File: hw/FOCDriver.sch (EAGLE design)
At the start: 111 parts, among them Q1 BC817, Q2 BC817, Q3 BC817, Q4 BC817, Q5 BC817, Q6 BC817, U1 IRF9389TRPBF, U2 IRF9389TRPBF, U3 LM27313XMF, U4 IRF9389TRPBF, U5 LM358N, U6 LM358N, U7 SN74LVC1G17, U8 SN74LVC1G17, U9 SN74LVC1G17

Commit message: layout
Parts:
- removed U7, U8, U9: SN74LVC1G17, SN74LVC1G17:SN74LVC1G17
- added U10, U11, U12: SN74LVC2G17, SN74LVC:SN74LVC2G17
- R17, R2, R9: value 100 -> 1K
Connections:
- new net N$49: R1.1, R3.1, U10G$2.Y
- new net N$50: R10.1, R8.1, U11G$2.Y
- new net N$51: R16.1, R18.1, U12G$2.Y
- net +5V: now also U10G$1.VCC, U11G$1.VCC, U12G$1.VCC; no longer U7.VCC, U8.VCC, U9.VCC
- net GND: now also U10G$1.GND, U11G$1.GND, U12G$1.GND; no longer U7.GND, U8.GND, U9.GND
- net H1: now also U10G$2.A; no longer R1.1, R3.1
- net H2: now also U11G$2.A; no longer R10.1, R8.1
- net H3: now also U12G$2.A; no longer R16.1, R18.1
- net L1: now also U10G$1.A; no longer U7.A
- net L2: now also U11G$1.A; no longer U8.A
- net L3: now also U12G$1.A; no longer U9.A
- net N$46: now also U10G$1.Y; no longer U7.Y
- net N$47: now also U11G$1.Y; no longer U8.Y
- net N$48: now also U12G$1.Y; no longer U9.Y
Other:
- moved on the sheet: C1, Q1, Q2, R1, R10, R17, R18, R2, R3, R4, R5, R6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

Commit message: layout
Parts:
- removed C9: 1nF, SparkFun-Capacitors:1.0UF-0805-25V-10%
- removed J1: (no value), SparkFun-Connectors:CONN_08"
- removed U2, U4: IRF9389TRPBF, IRF9389TRPBF:IRF9389TRPBF
- added C13: 47uF, rcl:CPOL-USE2.5-7
- added C14, C31: 0.1uF, SparkFun-Capacitors:1.0UF-0805-25V-10%
- added C2, C3, C6: 10uF, SparkFun-Capacitors:1.0UF-0805-25V-10%
- added C7: 100uF, rcl:CPOL-USE2.5-7
- added J3: (no value), SparkFun-Connectors:CONN_06SILK_FEMALE_PTH
- added U7, U8, U9: AO4606, AO4606:AO4606
- C10: value 4.7uF -> 0.1uF
- C11: value 470uF -> 47uF
- C19, C20: value 0.1uF -> 10uF
- R53: value 3.3K -> 1K
- U1: value IRF9389TRPBF -> SPX1117-5.0; device IRF9389TRPBF:IRF9389TRPBF -> SparkFun-IC-Power:V_REG_317SMD
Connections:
- removed net N$46: R2.1, U10G$1.Y
- removed net N$47: R9.1, U11G$1.Y
- removed net N$48: R17.1, U12G$1.Y
- removed net N$49: R1.1, R3.1, U10G$2.Y
- removed net N$50: R10.1, R8.1, U11G$2.Y
- removed net N$51: R16.1, R18.1, U12G$2.Y
- new net +3V3: J2.2, R54.E
- new net H1O: R1.1, R3.1, R45.2, U10G$2.Y
- new net H2O: R10.1, R49.2, R8.1, U11G$2.Y
- new net H3O: R16.1, R18.1, R51.2, U12G$2.Y
- new net L1O: R2.1, R46.2, U10G$1.Y
- new net L2O: R50.2, R9.1, U11G$1.Y
- new net L3O: R17.1, R52.2, U12G$1.Y
- net +12V: now also C31.1, U1.IN, U7A.S, U8A.S, U9A.S; no longer C9.1, U1A.S, U2A.S, U4A.S
- net +5V: now also C13.+, C14.1, C2.1, C3.1, C6.1, U1.OUT; no longer J2.1, R54.E
- net AGND: now also C13.-, C14.2, C31.2, C7.-, U1.ADJ; no longer C9.2
- net GND: now also C2.2, C3.2, C6.2, J2.1, J3.6; no longer J1.7, J1.8, J2.2
- net H1: no longer R45.2
- net H2: no longer R49.2
- net H3: no longer R51.2
- net ICOM: now also U9B.S; no longer U4B.S
- net IMOTORA: now also J3.3; no longer J1.3
- net IMOTORB: now also J3.2; no longer J1.2
- net IMOTORBUS: now also J3.1; no longer J1.1
- net IU: now also U7B.S; no longer U1B.S
- net IV: now also U8B.S; no longer U2B.S
- net L1: no longer R46.2
- net L2: no longer R50.2
- net L3: no longer R52.2
- net LEDJP1: now also J3.5; no longer J1.6
- net M1: now also U7A.D, U7B.D; no longer U1A.D, U1B.D
- net M2: now also U8A.D, U8B.D; no longer U2A.D, U2B.D
- net M3: now also U9A.D, U9B.D; no longer U4A.D, U4B.D
- net N$1: now also C7.+
- net N$10: now also U7A.G; no longer U1A.G
- net N$3: now also U9B.G; no longer U4B.G
- net N$6: now also U9A.G; no longer U4A.G
- net N$7: now also U8B.G; no longer U2B.G
- net N$8: now also U8A.G; no longer U2A.G
- net N$9: now also U7B.G; no longer U1B.G
- net POT: now also J3.4; no longer J1.5
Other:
- moved on the sheet: C1, C12, C5, C8, D1, F1, LED7, Q1, Q2, Q3, Q4, Q5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

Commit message: layout
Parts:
- removed C1, C12, C5: 10uF, SparkFun-Capacitors:1.0UF-0805-25V-10%
- removed C30: 0.1uF, SparkFun-Capacitors:1.0UF-0805-25V-10%
- removed C7: 100uF, rcl:CPOL-USE2.5-7
- removed C8: 220pF, SparkFun-Capacitors:1.0UF-0805-25V-10%
- removed L1: 10uH, resistor:L-USL3225M
- removed LED8: 12V, led:LEDSML0805
- removed R15: 118K, SparkFun-Resistors:RESISTOR0805
- removed R56: 10K, SparkFun-Resistors:RESISTOR0805
- removed U1: SPX1117-5.0, SparkFun-IC-Power:V_REG_317SMD
- removed U3: LM27313XMF, LM27313XMF:LM27313XMF
- added C32, C33: 220uF/100V, rcl:CPOL-USE5-10.5
- added J1: (no value), SparkFun-Connectors:CONN_02
- added Q7: IRFR5305, transistor-power:IRFR5305
- added U2: BA7805FP, SparkFun-IC-Power:V_REG_78XX7812
- C19, C2, C20, C3, C6: value 10uF -> 0.1uF
- C21, C22, C23: value 0.1uF -> 100pF
- C4: value 10uF -> 220uF/100V; device SparkFun-Capacitors:1.0UF-0805-25V-10% -> rcl:CPOL-USE5-10.5
- D1: value MBR0520LT -> MM3Z18VT1G; device diode:MBR0520LT -> SparkFun-DiscreteSemi:DIODE-ZENER-MM3Z3V3T1G
- F1: value 16V/4.00A -> 4A/30V
- R14: value 13.3K -> 22.6K
- R34, R35, R36, R37, R38, R39, R40, R41: value 30K 1% -> 20K 1%
- R53: value 1K -> 3.3K
- R54: value (none) -> 10K
- R55: value 1K -> 5.6K
- R7: value 51K -> 100K
- renumbered LED7 to 5VPWR
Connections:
- removed net +12V: C1.1, C10.1, C11.+, C12.1, C31.1, C5.1, C8.2, D1.C, R11.2, R15.2, R19.2, R4.2, R56.2, U1.IN, U7A.S, U8A.S, U9A.S
- removed net +3V3: J2.2, R54.E
- removed net N$29: C30.1, R54.A, R55.2
- removed net N$45: LED8.A, R56.1
- removed net N$5 (its old number): D1.A, L1.1, U3.SW
- new net VCC: C10.1, C11.+, C31.1, C32.+, C33.+, C4.+, D1.C, J1.2, Q7.S, R11.2, R19.2, R4.2, R7.2, U2.IN, U7A.S, U8A.S, U9A.S
- net +5V: now also R55.2, U2.OUT; no longer U1.OUT
- net AGND: now also C32.-, C33.-, C4.-, U2.GND; no longer C21.2, C22.2, C23.2, C4.2, C7.-, LED8.C, U1.ADJ, U3.GND
- net GND: now also J2.2, R54.A; no longer C30.2, R55.1
- net N$1: now also J1.1, Q7.D; no longer C4.1, C7.+, L1.2, R7.1, U3.VIN
- net N$10: no longer C1.2
- net N$15: now also C21.2
- net N$2: now also D1.A, Q7.G, R14.2, R7.1; no longer R7.2, U3.!SHDN!
- net N$20: now also C22.2
- net N$25: now also C23.2
- net N$4: now also R54.E, R55.1; no longer C8.1, R14.2, R15.1, U3.FB
- net N$6: no longer C12.2
- net N$8: no longer C5.2
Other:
- note added: "0~3.2V"
- note added: "Gain: I * 0.025 * 20k / 1k = 0.5 V/A FS Current = 2.5V / 0.5V/A = +/-5A F = 1/ 2 * Pi * 20k * 100pF"
- note added: "VREF: 5V * 20k / 40k = 2.5V F = 1/ 2 * Pi * 20k||20k * 100nF"
- moved on the sheet: C10, C11, C13, C14, C18, C21, C22, C23, C31, D1, F1, R14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

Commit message: layout
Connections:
- new net VDD: C19.1, U5G$3.VCC
- net AVDD: no longer C19.1, U5G$3.VCC
- net N$19: now also U6G$1.-IN; no longer U5G$1.-IN
- net N$20: now also U6G$1.+IN; no longer U5G$1.+IN
- net N$21: now also U6G$1.OUT; no longer U5G$1.OUT
- net N$24: now also U5G$1.-IN; no longer U6G$1.-IN
- net N$25: now also U5G$1.+IN; no longer U6G$1.+IN
- net N$26: now also U5G$1.OUT; no longer U6G$1.OUT
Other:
- moved on the sheet: C16, C17, C20, C21, C22, C25, C26, R24, R25, R26, R27, R30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

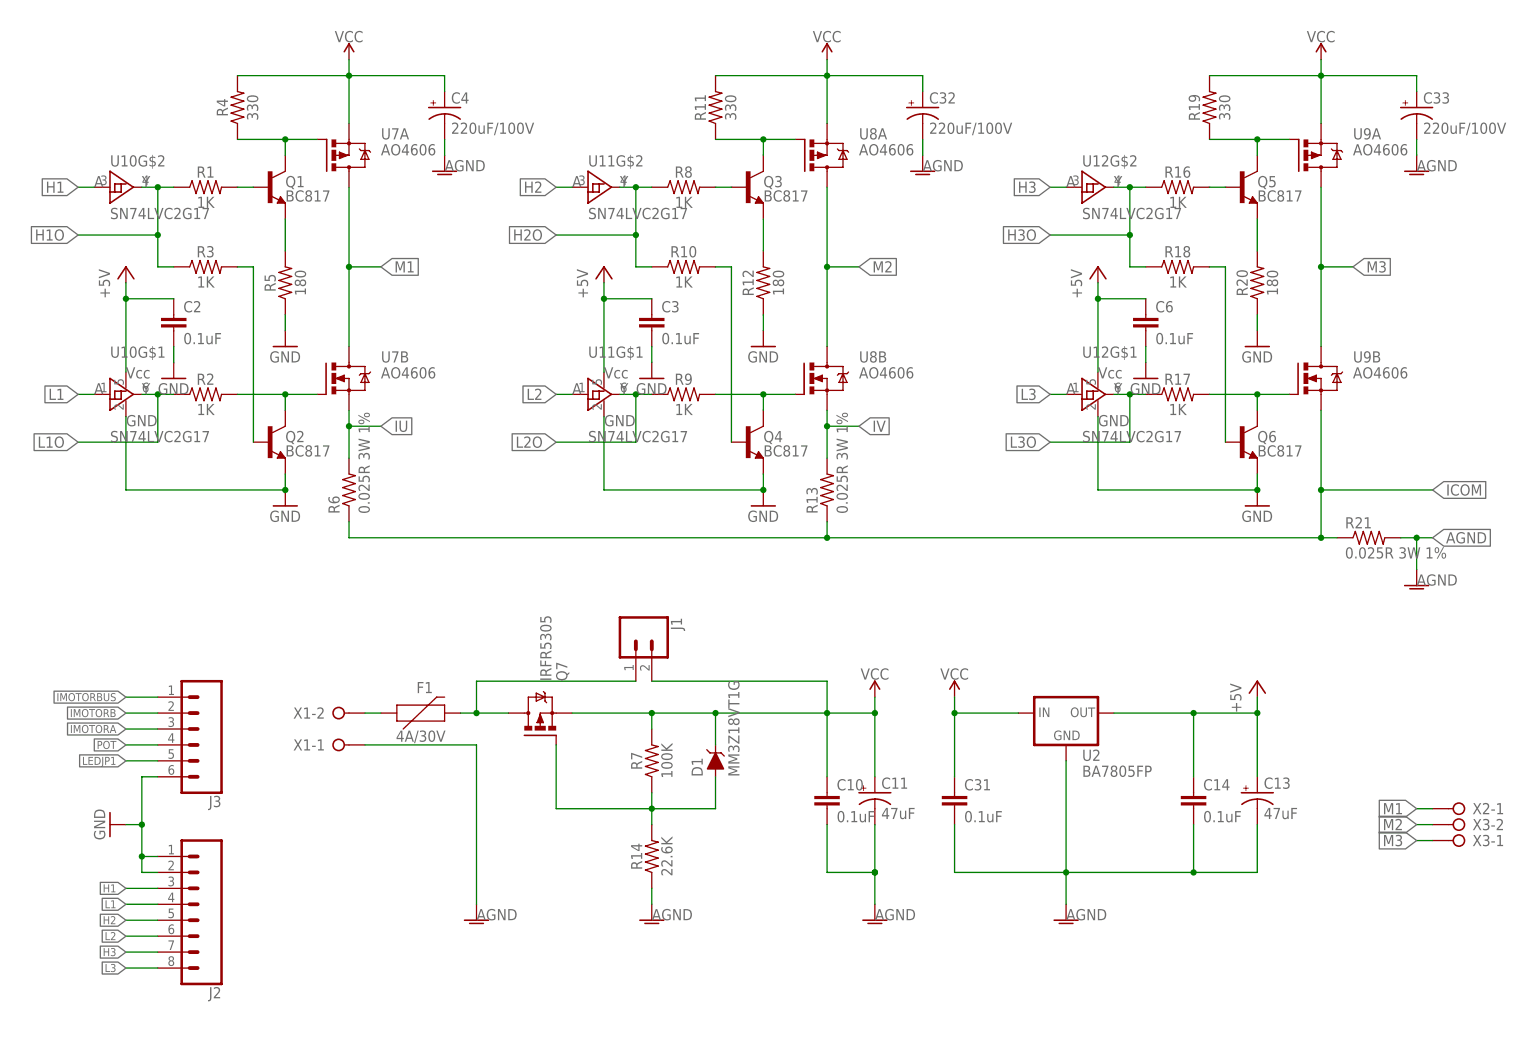
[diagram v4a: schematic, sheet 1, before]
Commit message: change power conn
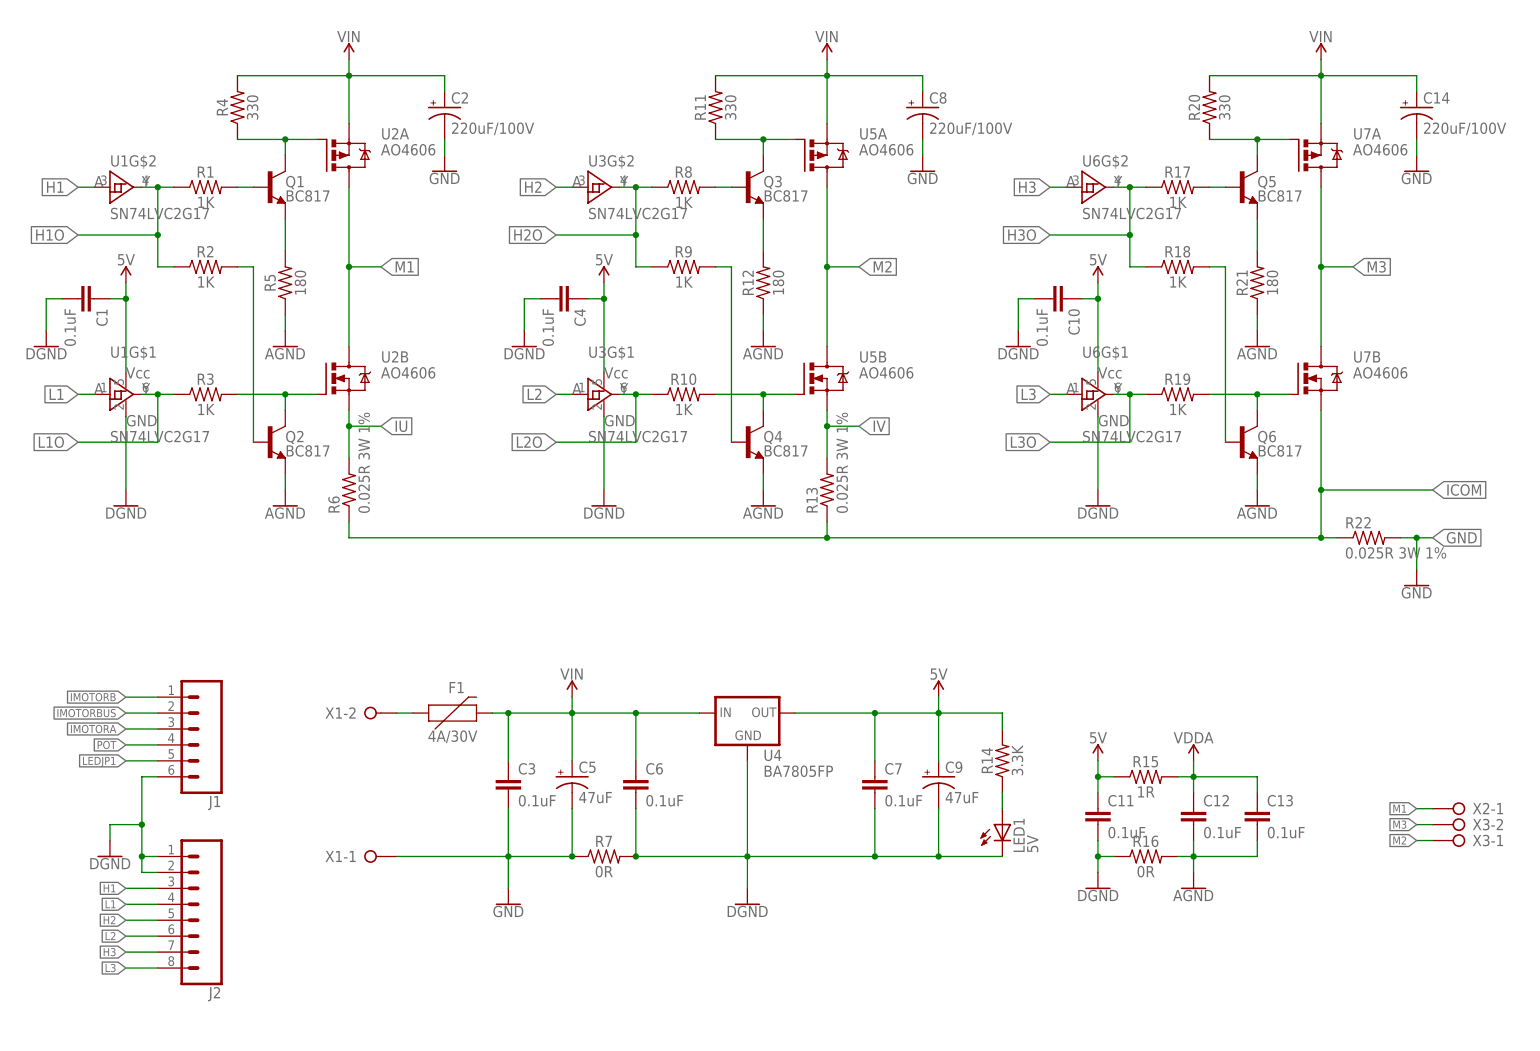
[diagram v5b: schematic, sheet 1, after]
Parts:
- removed 5VPWR: 5V, led:LEDSML0805
- removed C27, C28, C29, C31: 0.1uF, SparkFun-Capacitors:1.0UF-0805-25V-10%
- removed C33: 220uF/100V, rcl:CPOL-USE5-10.5
- removed D1: MM3Z18VT1G, SparkFun-DiscreteSemi:DIODE-ZENER-MM3Z3V3T1G
- removed J3: (no value), SparkFun-Connectors:CONN_06SILK_FEMALE_PTH
- removed Q7: IRFR5305, transistor-power:IRFR5305
- removed R54: 10K, pot:TRIM_US-CT6
- removed R55: 5.6K, SparkFun-Resistors:RESISTOR0805
- removed U12: SN74LVC2G17, SN74LVC:SN74LVC2G17
- added C1, C12, C7: 0.1uF, SparkFun-Capacitors:1.0UF-0805-25V-10%
- added C5, C9: 47uF, rcl:CPOL-USE2.5-7
- added LED7: (no value), led:LEDSML0805
- added R15: 1R, SparkFun-Resistors:RESISTOR0805
- added U4: BA7805FP, SparkFun-IC-Power:V_REG_78XX7812
- C11, C13: value 47uF -> 0.1uF; device rcl:CPOL-USE2.5-7 -> SparkFun-Capacitors:1.0UF-0805-25V-10%
- C14, C2: value 0.1uF -> 220uF/100V; device SparkFun-Capacitors:1.0UF-0805-25V-10% -> rcl:CPOL-USE5-10.5
- C4: value 220uF/100V -> 0.1uF; device rcl:CPOL-USE5-10.5 -> SparkFun-Capacitors:1.0UF-0805-25V-10%
- J1: device SparkFun-Connectors:CONN_02 -> SparkFun-Connectors:CONN_06SILK_FEMALE_PTH
- LED1: value (none) -> 5V
- R14: value 22.6K -> 3.3K
- R16: value 1K -> 0R
- R19: value 330 -> 1K
- R20: value 180 -> 330
- R21: value 0.025R 3W 1% -> 180; device resistor:R-US_R2512 -> SparkFun-Resistors:RESISTOR0805
- R22: value 1K 1% -> 0.025R 3W 1%; device SparkFun-Resistors:RESISTOR0805 -> resistor:R-US_R2512
- R34: value 20K 1% -> 1K 1%
- R42: value 1K 1% -> 20K 1%
- R45: value 1K -> 1K 1%
- R46: value 1K -> 5.6K
- R47: value 1R -> 10K; device SparkFun-Resistors:RESISTOR0805 -> pot:TRIM_US-CT6
- R48: value 0R -> 1K
- R53: value 3.3K -> 1K
- R7: value 100K -> 0R
- U2: value BA7805FP -> AO4606; device SparkFun-IC-Power:V_REG_78XX7812 -> AO4606:AO4606
- U5: value LM358N -> AO4606; device Fairchild-LM358N:LM358N -> AO4606:AO4606
- U6: value LM358N -> SN74LVC2G17; device Fairchild-LM358N:LM358N -> SN74LVC:SN74LVC2G17
- U8, U9: value AO4606 -> LM358N; device AO4606:AO4606 -> Fairchild-LM358N:LM358N
- renumbered C32 to C8, U10 to U1, U11 to U3
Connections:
- removed net +5V: C13.+, C14.1, C2.1, C27.1, C3.1, C6.1, R47.1, R53.2, R55.2, U12G$1.VCC, U1G$1.VCC, U2.OUT, U3G$1.VCC
- removed net AVDD: C20.1, C28.1, C29.1, R34.2, R47.2, U6G$3.VCC
- removed net N$1: F1.2, J1.1, Q7.D
- removed net N$2: D1.A, Q7.G, R14.2, R7.1
- removed net N$34 (its old number): LED2.A, R46.1
- removed net VCC: C10.1, C11.+, C31.1, C33.+, C4.+, C8.+, D1.C, J1.2, Q7.S, R11.2, R19.2, R4.2, R7.2, U2.IN, U7A.S, U8A.S, U9A.S
- removed net VDD: C19.1, U5G$3.VCC
- new net 5V: C1.1, C10.1, C11.1, C4.1, C7.1, C9.+, R14.2, R15.1, R46.2, U1G$1.VCC, U3G$1.VCC, U4.OUT, U6G$1.VCC
- new net DGND: C1.2, C10.2, C11.2, C4.2, C6.2, C7.2, C9.-, J1.6, J2.1, J2.2, LED1.C, R16.1, R47.A, R7.2, U1G$1.GND, U3G$1.GND, U4.GND, U6G$1.GND
- new net N$38: LED7.A, R53.1
- new net VDDA: C12.1, C13.1, C19.1, C20.1, R15.2, R35.2, U8G$3.VCC, U9G$3.VCC
- new net VIN: C14.+, C2.+, C3.1, C5.+, C6.1, C8.+, F1.2, R11.2, R20.2, R4.2, U2A.S, U4.IN, U5A.S, U7A.S
- net AGND: now also C12.2, C13.2, Q2.E, Q4.E, Q6.E, R12.1, R16.2, R21.1, R36.1, R5.1, U8G$3.GND, U9G$3.GND; no longer C10.2, C11.-, C13.-, C14.2, C28.2, C29.2, C31.2, C33.-, C4.-, C8.-, R14.1, R21.2, R26.1, R35.1, R48.2, U2.GND, U5G$3.GND, U6G$3.GND, X1-1.KL
- net GND: now also C14.-, C2.-, C5.-, C8.-, R22.2, R27.1, R7.1, X1-1.KL; no longer 5VPWR.C, C2.2, C27.2, C6.2, J2.1, J2.2, J3.6, Q2.E, Q4.E, Q6.E, R12.1, R20.1, R48.1, R5.1, R54.A, U12G$1.GND, U1G$1.GND, U3G$1.GND
- net H1O: now also R2.1, R48.2; no longer R3.1, R45.2
- net H2O: now also R50.2, R9.1; no longer R10.1, R49.2
- net H3: now also U6G$2.A; no longer U12G$2.A
- net H3O: now also R17.1, R52.2, U6G$2.Y; no longer R16.1, R51.2, U12G$2.Y
- net ICOM: now also R23.1, R25.1, R28.1, U7B.S; no longer R21.1, R24.1, R27.1, U9B.S
- net IMOTORA: now also J1.3, R43.2; no longer J3.3, R42.2
- net IMOTORB: now also J1.1, R44.2; no longer J3.2, R43.2
- net IMOTORBUS: now also J1.2, R45.2; no longer J3.1, R44.2
- net IU: now also R24.1, U2B.S; no longer R23.1, U7B.S
- net IV: now also R26.1, U5B.S; no longer R25.1, U8B.S
- net L1O: now also R3.1, R49.2; no longer R2.1, R46.2
- net L2O: now also R10.1, R51.2; no longer R50.2, R9.1
- net L3: now also U6G$1.A; no longer U12G$1.A
- net L3O: now also R19.1, R53.2, U6G$1.Y; no longer R17.1, R52.2, U12G$1.Y
- net LEDJP1: now also J1.5, LED7.C; no longer J3.5, LED1.C
- net M1: now also U2A.D, U2B.D; no longer U7A.D, U7B.D
- net M2: now also U5A.D, U5B.D, X3-1.KL; no longer U8A.D, U8B.D, X3-2.KL
- net M3: now also U7A.D, U7B.D, X3-2.KL; no longer U9A.D, U9B.D, X3-1.KL
- net N$10: now also U2A.G; no longer U7A.G
- net N$11: now also R23.2, R29.1; no longer R22.2, R28.1
- net N$12: now also R24.2, R30.1; no longer R23.2, R29.1
- net N$13: now also R29.2, R37.1, U9G$2.-IN; no longer R28.2, R36.1, U5G$2.-IN
- net N$14: now also R25.2, R31.1; no longer R24.2, R30.1
- net N$15: now also R30.2, R41.1, U9G$2.+IN; no longer R29.2, R39.1, U5G$2.+IN
- net N$16: now also R37.2, R43.1, U9G$2.OUT; no longer R36.2, R42.1, U5G$2.OUT
- net N$17: now also R26.2, R32.1; no longer R25.2, R31.1
- net N$18: now also R35.1, R36.2, U8G$2.+IN; no longer R34.1, R35.2, U6G$2.+IN
- net N$19: now also R31.2, R38.1, U8G$1.-IN; no longer R30.2, R37.1, U6G$1.-IN
- net N$20: now also R32.2, R42.1, U8G$1.+IN; no longer R31.2, R40.1, U6G$1.+IN
- net N$21: now also R38.2, R44.1, U8G$1.OUT; no longer R37.2, R43.1, U6G$1.OUT
- net N$22: now also R27.2, R33.1; no longer R26.2, R32.1
- net N$23: now also R28.2, R34.1; no longer R27.2, R33.1
- net N$24: now also R33.2, R39.1, U9G$1.-IN; no longer R32.2, R38.1, U5G$1.-IN
- net N$25: now also R34.2, R40.1, U9G$1.+IN; no longer R33.2, R41.1, U5G$1.+IN
- net N$26: now also R39.2, R45.1, U9G$1.OUT; no longer R38.2, R44.1, U5G$1.OUT
- net N$28: now also R21.2; no longer R20.2
- net N$3: now also R19.2, U7B.G; no longer R17.2, U9B.G
- net N$31: now also LED1.A, R14.1; no longer 5VPWR.A, R53.1
- net N$32: now also R2.2; no longer R3.2
- net N$33: now also LED2.A, R48.1; no longer LED1.A, R45.1
- net N$4: now also R46.1, R47.E; no longer R54.E, R55.1
- net N$41: now also R9.2; no longer R10.2
- net N$42: now also R17.2; no longer R16.2
- net N$6: now also R20.1, U7A.G; no longer R19.1, U9A.G
- net N$7: now also R10.2, U5B.G; no longer R9.2, U8B.G
- net N$8: now also U5A.G; no longer U8A.G
- net N$9: now also R3.2, U2B.G; no longer R2.2, U7B.G
- net POT: now also J1.4, R47.S; no longer J3.4, R54.S
- net VREF: now also R42.2, U8G$2.-IN, U8G$2.OUT; no longer R39.2, U6G$2.-IN, U6G$2.OUT
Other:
- moved on the sheet: C10, C3, C6, F1, LED2, LED3, LED4, LED5, LED6, R10, R14, R16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

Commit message: layout
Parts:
- removed J2: (no value), SparkFun-Connectors:CONN_08"
- added J3: (no value), SparkFun-Connectors:CONN_06SILK_FEMALE_PTH
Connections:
- net DGND: no longer J2.1, J2.2
- net H1: now also J3.2; no longer J2.3
- net H2: now also J3.4; no longer J2.5
- net H3: now also J3.6; no longer J2.7
- net L1: now also J3.1; no longer J2.4
- net L2: now also J3.3; no longer J2.6
- net L3: now also J3.5; no longer J2.8
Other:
- moved on the sheet: C11, C12, C13, R15
